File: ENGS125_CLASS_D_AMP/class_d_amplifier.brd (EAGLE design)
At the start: 100 x 80 mm, 21 parts, among them J1 BANANA_JACK_CT3151, J2 BANANA_JACK_CT3151, J3 BANANA_JACK_CT3151, J4 BANANA_JACK_CT3151, J5 BANANA_JACK_CT3151, J6 BANANA_JACK_CT3151, M1 AUIRLR024ZTRL, M2 AUIRLR024ZTRL, U1 LTC6992TSOT-23, U2 LTC4449

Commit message: Replaced Rset with trim potentiometer
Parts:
- R1: value 100kΩ -> (none); device Engs125_library:R0805 -> Engs125_lib_UPDATEFeb22:CT6
- moved R1 29.5 mm to (-10.2, -21.6)
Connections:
- net GND: now also R1.E; no longer R1.1
- net N$1: now also R1.A; no longer R1.2
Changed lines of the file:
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@@
 <attribute name="VALUE" x="32.86" y="47.42" size="1.016" layer="27" rot="R90"/>
-</element>
-<element name="R1" library="Engs125_library" package="R0805" value="100kΩ" x="19.05" y="-17.78" smashed="yes">
-<attribute name="NAME" x="18.415" y="-16.51" size="1.27" layer="25"/>
-<attribute name="VALUE" x="18.415" y="-20.32" size="1.27" layer="27"/>
 </element>
 <element name="U2" library="Engs125_library" package="DCB8" value="LTC4449" x="58.42" y="19.05" smashed="yes" rot="R90">
@@
 <attribute name="VALUE" x="0.3175" y="-26.9875" size="1.016" layer="27" ratio="10" rot="R90"/>
 </element>
+<element name="R1" library="Engs125_lib_UPDATEFeb22" package="CT6" value="" x="-10.16" y="-21.59" smashed="yes">
+<attribute name="NAME" x="-13.462" y="-17.653" size="1.27" layer="25" ratio="10"/>
+<attribute name="VALUE" x="-13.4366" y="-26.797" size="1.27" layer="27" ratio="10"/>
+</element>
 </elements>
 <signals>
 <signal name="N$1">
-<contactref element="R1" pad="2"/>
 <contactref element="U1" pad="3"/>
-<wire x1="20" y1="-17.78" x2="-1.59" y2="-26.7" width="0" layer="19" extent="1-1"/>
+<contactref element="R1" pad="A"/>
+<wire x1="-1.59" y1="-26.7" x2="-7.6454" y2="-21.59" width="0" layer="19" extent="1-1"/>
 </signal>
 <signal name="GND">
-<contactref element="R1" pad="1"/>
 <contactref element="C3" pad="2"/>
 <contactref element="C4" pad="2"/>
@@
 <contactref element="J6" pad="P$2"/>
 <contactref element="U1" pad="4"/>
+<contactref element="R1" pad="E"/>
 <wire x1="87.62" y1="53.35" x2="92.72" y2="53.35" width="0" layer="19" extent="1-1"/>
 <wire x1="92.72" y1="48.25" x2="92.72" y2="53.35" width="0" layer="19" extent="1-1"/>
@@
 <wire x1="12.38" y1="-10.16" x2="17.46" y2="-10.16" width="0" layer="19" extent="1-1"/>
 <wire x1="7.3" y1="-10.16" x2="12.38" y2="-10.16" width="0" layer="19" extent="1-1"/>
-<wire x1="18.1" y1="-17.78" x2="17.46" y2="-10.16" width="0" layer="19" extent="1-1"/>
-<wire x1="14.1" y1="-17.78" x2="18.1" y2="-17.78" width="0" layer="19" extent="1-1"/>
+<wire x1="14.1" y1="-17.78" x2="12.38" y2="-10.16" width="0" layer="19" extent="1-1"/>
 <wire x1="2.67" y1="-17.78" x2="7.3" y2="-10.16" width="0" layer="19" extent="1-1"/>
 <wire x1="-2.86" y1="-17.78" x2="2.67" y2="-17.78" width="0" layer="19" extent="1-1"/>
 <wire x1="-1.59" y1="-24.1" x2="-2.86" y2="-17.78" width="0" layer="19" extent="1-1"/>
+<wire x1="-12.6746" y1="-21.59" x2="-2.86" y2="-17.78" width="0" layer="19" extent="1-1"/>
 <wire x1="30.24" y1="42.63" x2="58.42" y2="19.05" width="0" layer="19" extent="1-1"/>
 <wire x1="12.71" y1="33.03" x2="30.24" y2="42.63" width="0" layer="19" extent="1-1"/>

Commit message: Added pin header for PWM output probe
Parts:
- added JP2: (no value), Engs125_lib_UPDATEFeb22:1X01
- added R2: (no value), Engs125_lib_UPDATEFeb22:R0805
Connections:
- removed net VREF: JP1.1, U1.1
- new net N$4: R2.2, U1.1
- net GND: now also JP1.1, R2.1
- net VPWM: now also JP2.1
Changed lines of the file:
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@@
 <attribute name="VALUE" x="-13.4366" y="-26.797" size="1.27" layer="27" ratio="10"/>
+</element>
+<element name="R2" library="Engs125_lib_UPDATEFeb22" package="R0805" value="" x="-11.43" y="-30.48" smashed="yes">
+<attribute name="NAME" x="-12.192" y="-29.464" size="1.27" layer="25"/>
+<attribute name="VALUE" x="-12.192" y="-32.766" size="1.27" layer="27"/>
+</element>
+<element name="JP2" library="Engs125_lib_UPDATEFeb22" package="1X01" value="" x="-11.43" y="-35.56" smashed="yes">
+<attribute name="NAME" x="-12.7762" y="-33.7312" size="1.27" layer="25" ratio="10"/>
+<attribute name="VALUE" x="-12.7" y="-38.735" size="1.27" layer="27"/>
 </element>
 </elements>
@@
 <contactref element="U2" pad="4"/>
 <contactref element="U2" pad="9"/>
-<contactref element="JP1" pad="2"/>
 <contactref element="J2" pad="P$4"/>
 <contactref element="J2" pad="P$1"/>
@@
 <contactref element="U1" pad="4"/>
 <contactref element="R1" pad="E"/>
+<contactref element="JP1" pad="1"/>
+<contactref element="JP1" pad="2"/>
+<contactref element="R2" pad="1"/>
 <wire x1="87.62" y1="53.35" x2="92.72" y2="53.35" width="0" layer="19" extent="1-1"/>
 <wire x1="92.72" y1="48.25" x2="92.72" y2="53.35" width="0" layer="19" extent="1-1"/>
@@
 <wire x1="59.82" y1="19.725" x2="87.62" y2="48.25" width="0" layer="19" extent="1-1"/>
 <wire x1="58.42" y1="19.05" x2="59.82" y2="19.725" width="0" layer="19" extent="1-1"/>
-<wire x1="46.99" y1="5.08" x2="58.42" y2="19.05" width="0" layer="19" extent="1-1"/>
+<wire x1="49.53" y1="5.08" x2="58.42" y2="19.05" width="0" layer="19" extent="1-1"/>
+<wire x1="46.99" y1="5.08" x2="49.53" y2="5.08" width="0" layer="19" extent="1-1"/>
 <wire x1="17.46" y1="-10.16" x2="46.99" y2="5.08" width="0" layer="19" extent="1-1"/>
 <wire x1="12.38" y1="-10.16" x2="17.46" y2="-10.16" width="0" layer="19" extent="1-1"/>
@@
 <wire x1="-1.59" y1="-24.1" x2="-2.86" y2="-17.78" width="0" layer="19" extent="1-1"/>
 <wire x1="-12.6746" y1="-21.59" x2="-2.86" y2="-17.78" width="0" layer="19" extent="1-1"/>
+<wire x1="-12.28" y1="-30.48" x2="-12.6746" y2="-21.59" width="0" layer="19" extent="1-1"/>
 <wire x1="30.24" y1="42.63" x2="58.42" y2="19.05" width="0" layer="19" extent="1-1"/>
 <wire x1="12.71" y1="33.03" x2="30.24" y2="42.63" width="0" layer="19" extent="1-1"/>
@@
 <contactref element="U2" pad="5"/>
 <contactref element="U1" pad="6"/>
+<contactref element="JP2" pad="1"/>
 <wire x1="-3.49" y1="-24.1" x2="57.02" y2="19.725" width="0" layer="19" extent="1-1"/>
+<wire x1="-11.43" y1="-35.56" x2="-3.49" y2="-24.1" width="0" layer="19" extent="1-1"/>
 </signal>
 <signal name="N$2">
@@
 <wire x1="59.82" y1="18.375" x2="25.64" y2="27.39" width="0" layer="19" extent="1-1"/>
 </signal>
-<signal name="VREF">
-<contactref element="JP1" pad="1"/>
-<contactref element="U1" pad="1"/>
-<wire x1="-3.49" y1="-26.7" x2="49.53" y2="5.08" width="0" layer="19" extent="1-1"/>
-</signal>
 <signal name="N$3">
 <contactref element="U1" pad="2"/>
 </signal>
+<signal name="N$4">
+<contactref element="U1" pad="1"/>
+<contactref element="R2" pad="2"/>
+<wire x1="-3.49" y1="-26.7" x2="-10.58" y2="-30.48" width="0" layer="19" extent="1-1"/>
+</signal>
 </signals>

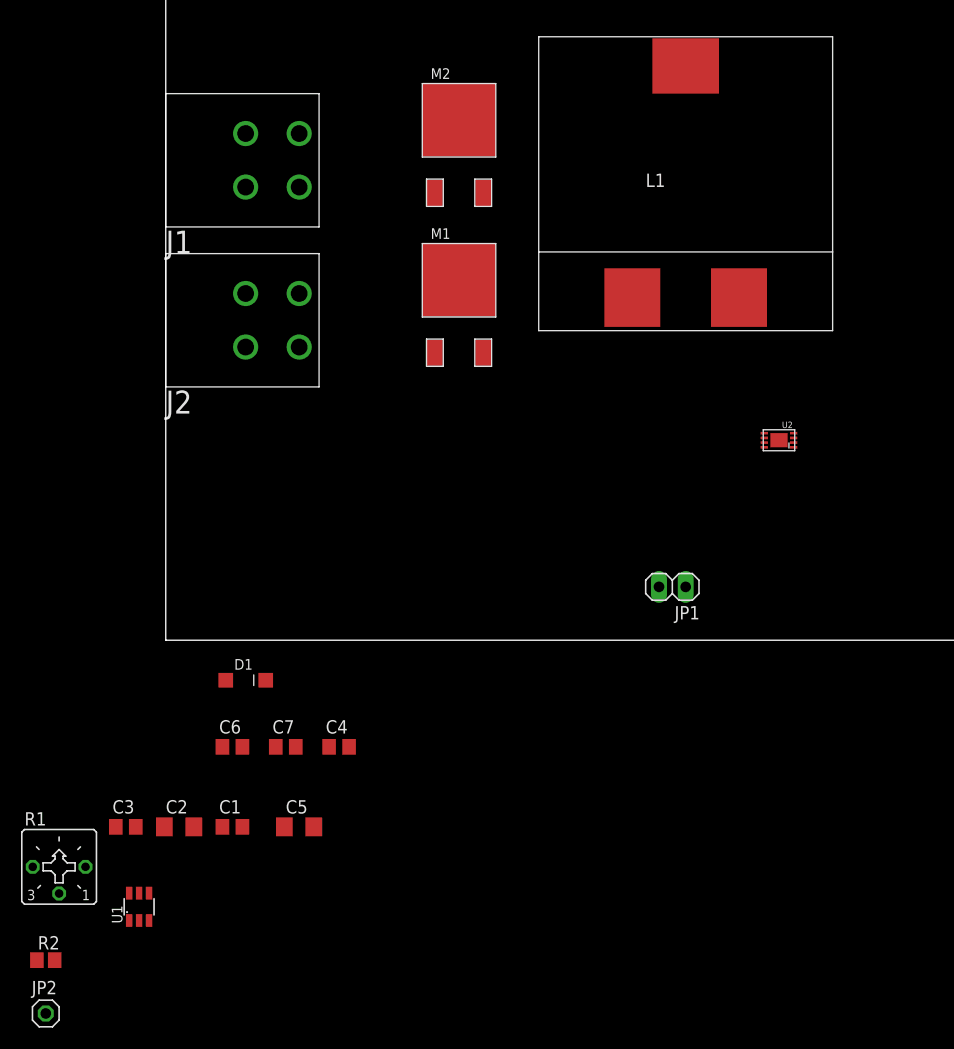
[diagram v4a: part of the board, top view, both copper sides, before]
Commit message: Added footprint for switch. Added switch to schematic.
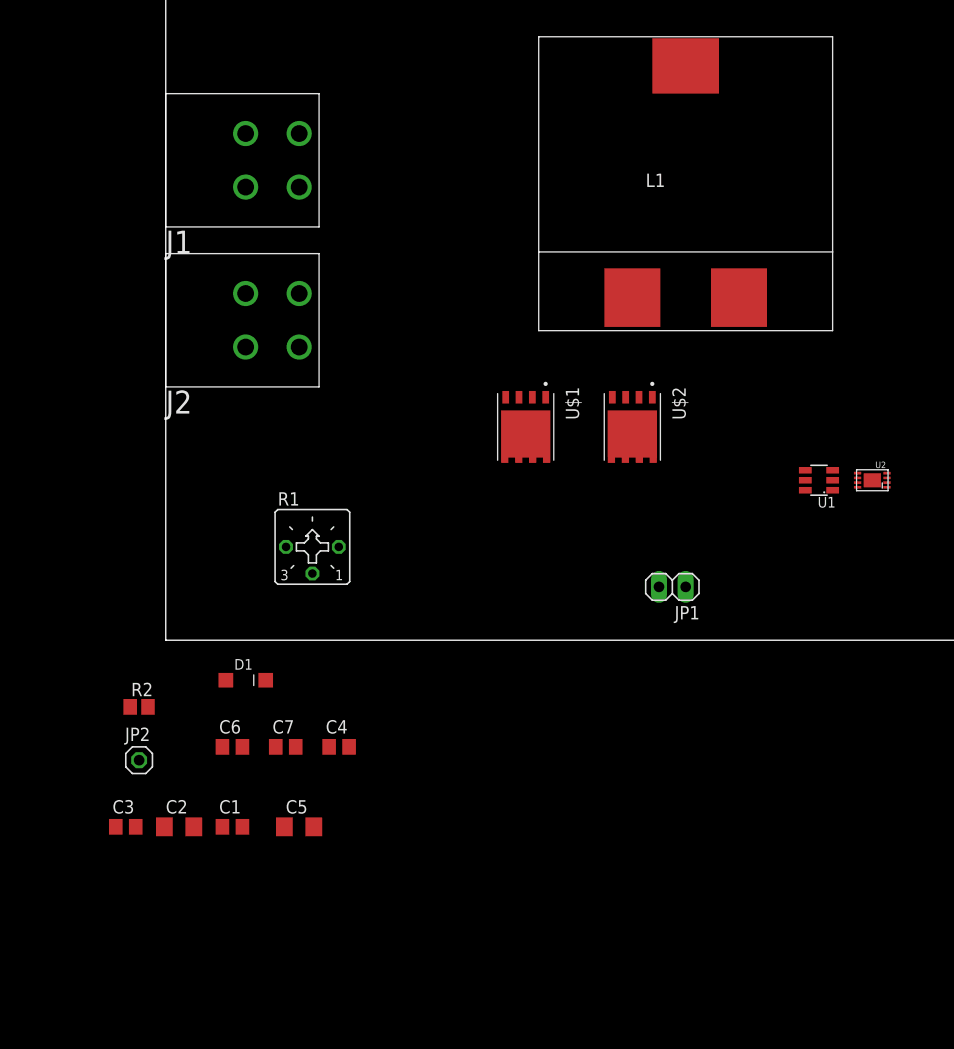
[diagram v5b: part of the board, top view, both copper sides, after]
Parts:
- removed M1, M2: AUIRLR024ZTRL, Engs125_library:DPAK
- added U$1, U$2: BSC050NE2LSATMA1, Engs125_lib_UPDATEFeb22:PG-TDSON-8
- moved U1 76.5 mm to (62.2, 15.2), turned to 90 degrees
- moved R1 38.9 mm to (14.0, 8.89)
- moved JP2 25.7 mm to (-2.54, -11.4)
- moved R2 25.7 mm to (-2.54, -6.35)
- moved U2 9.67 mm to (67.3, 15.2)
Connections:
- net BG: now also U$2.4; no longer M2.G
- net GND: now also U$2.1, U$2.2, U$2.3; no longer M2.S
- net TG: now also U$1.4; no longer M1.G
- net VIN: now also U$1.5, U$1.8, U$1.9; no longer M1.D
- net VSW: now also U$1.1, U$1.2, U$1.3, U$2.5, U$2.8, U$2.9; no longer M1.S, M2.D

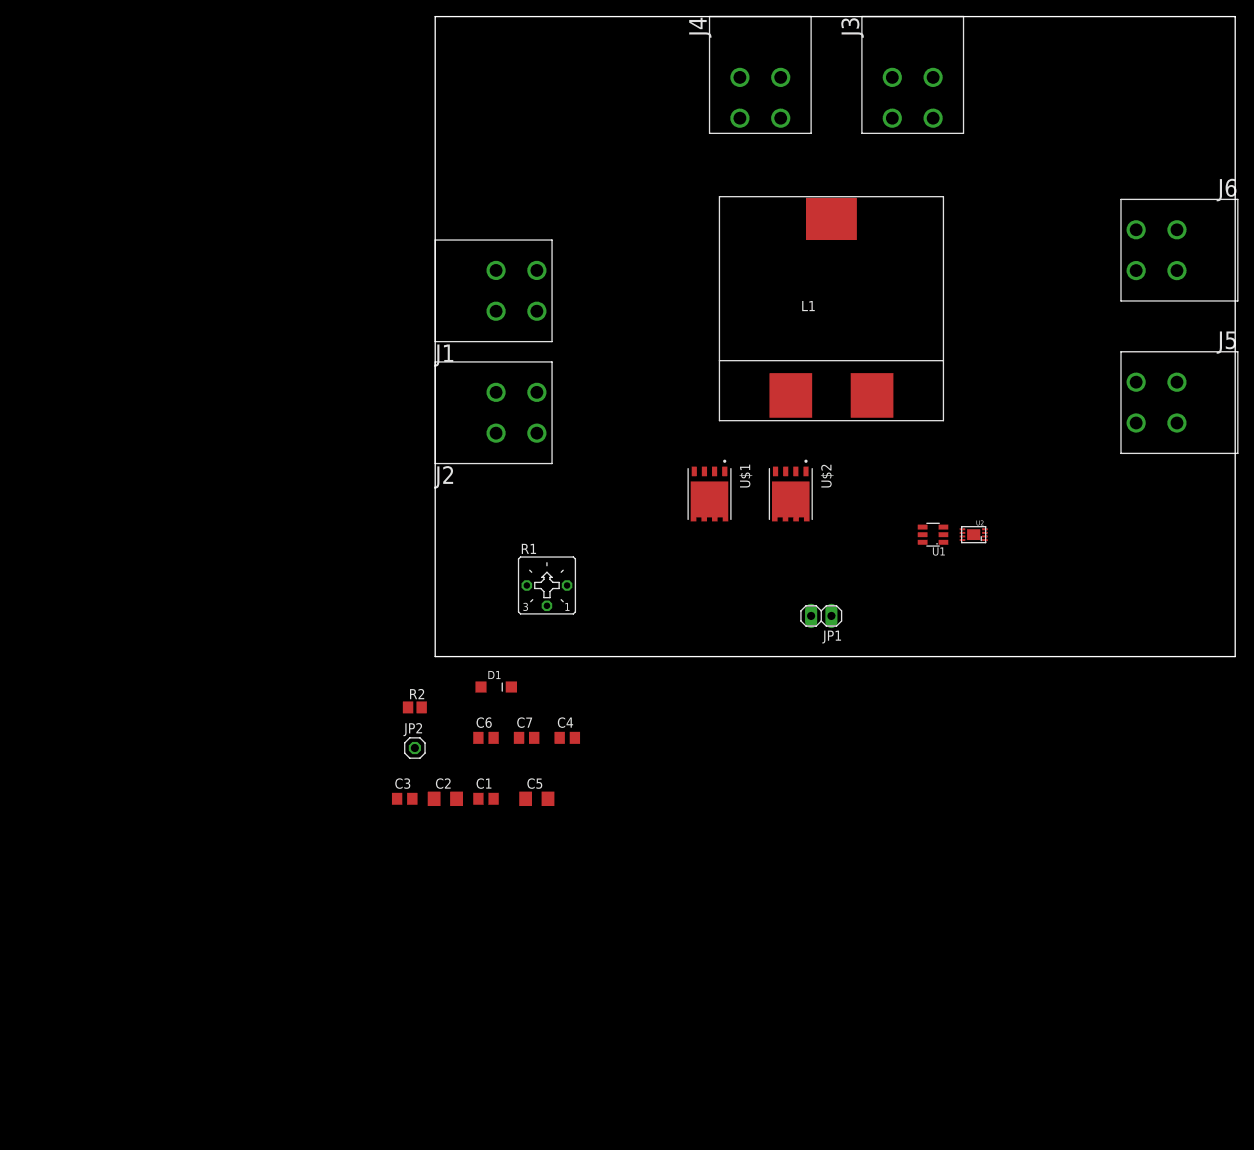
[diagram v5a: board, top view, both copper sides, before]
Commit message: Initial placement of switching node components
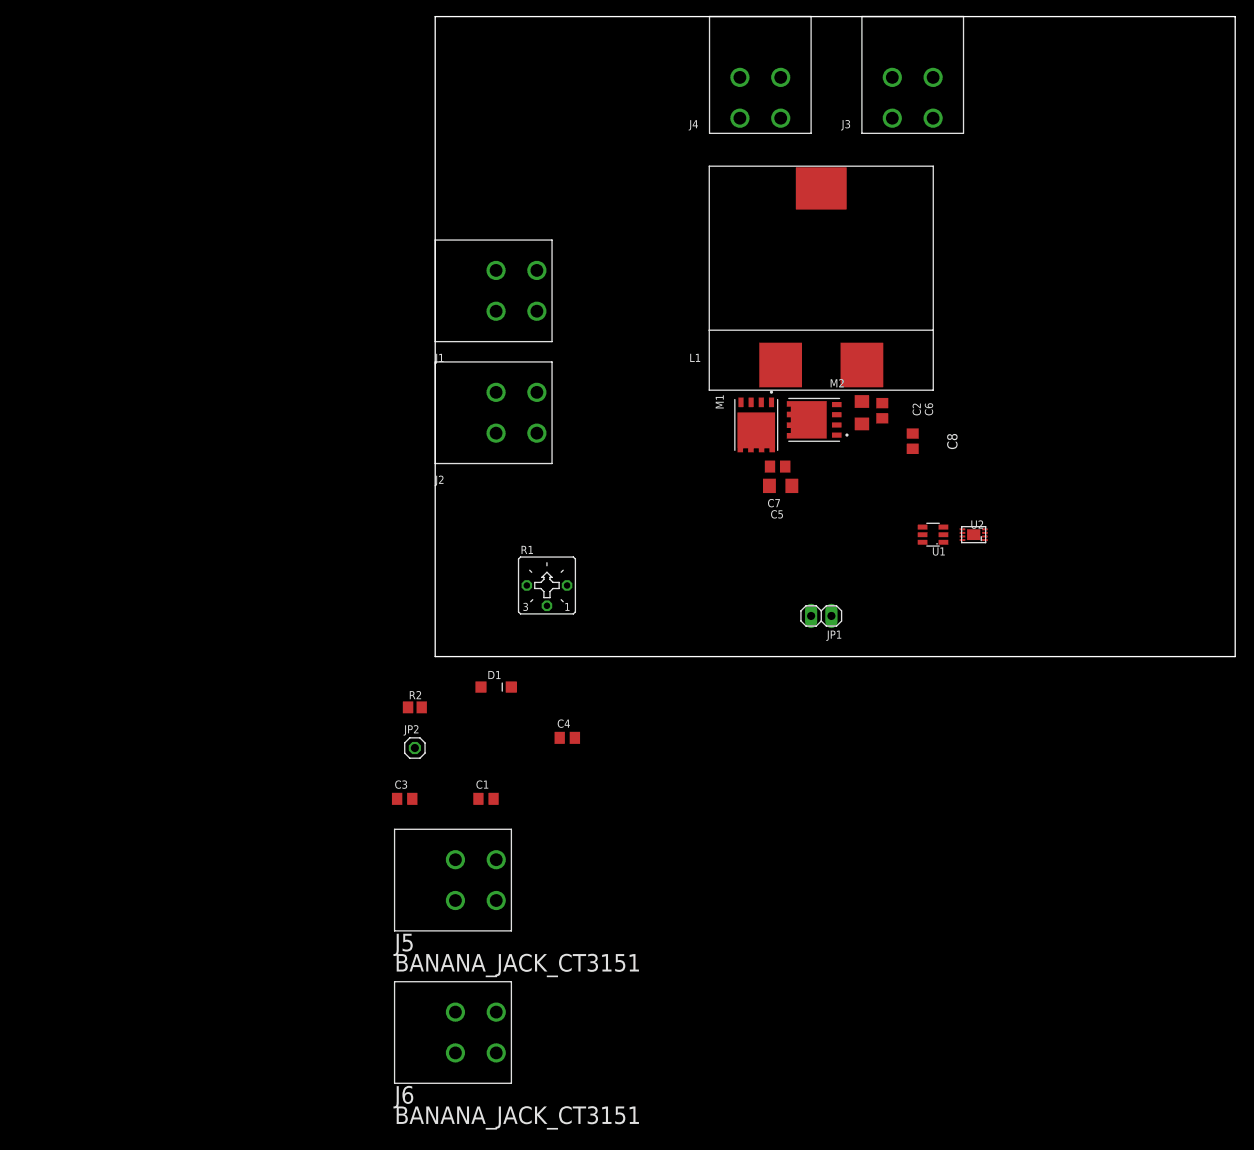
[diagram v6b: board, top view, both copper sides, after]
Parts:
- removed U$1, U$2: BSC050NE2LSATMA1, Engs125_lib_UPDATEFeb22:PG-TDSON-8
- added C8: 0.1u, Engs125_library:C0805
- added M1, M2: BSC050NE2LSATMA1, Engs125_lib_UPDATEFeb22:PG-TDSON-8
- moved J6 129.6 mm to (5.08, -47.0), turned to 0 degrees
- moved J5 103.9 mm to (5.08, -27.9), turned to 0 degrees
- moved C2 71.0 mm to (53.3, 30.5), turned to 270 degrees
- moved C6 64.2 mm to (55.9, 30.7), turned to 270 degrees
- moved C5 49.6 mm to (43.2, 21.3)
- moved C7 46.2 mm to (42.8, 23.7)
- moved L1 4.02 mm to (48.3, 50.8)
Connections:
- net BG: now also M2.4; no longer U$2.4
- net GND: now also C8.2, M2.1, M2.2, M2.3; no longer U$2.1, U$2.2, U$2.3
- net TG: now also M1.4; no longer U$1.4
- net VIN: now also M1.5, M1.8, M1.9; no longer U$1.5, U$1.8, U$1.9
- net VOUT: now also C8.1
- net VSW: now also M1.1, M1.2, M1.3, M2.5, M2.8, M2.9; no longer U$1.1, U$1.2, U$1.3, U$2.5, U$2.8, U$2.9
